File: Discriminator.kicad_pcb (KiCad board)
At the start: 2 copper layers, 29 parts, among them U1 PSA4-5043+, U2 PGA-103+

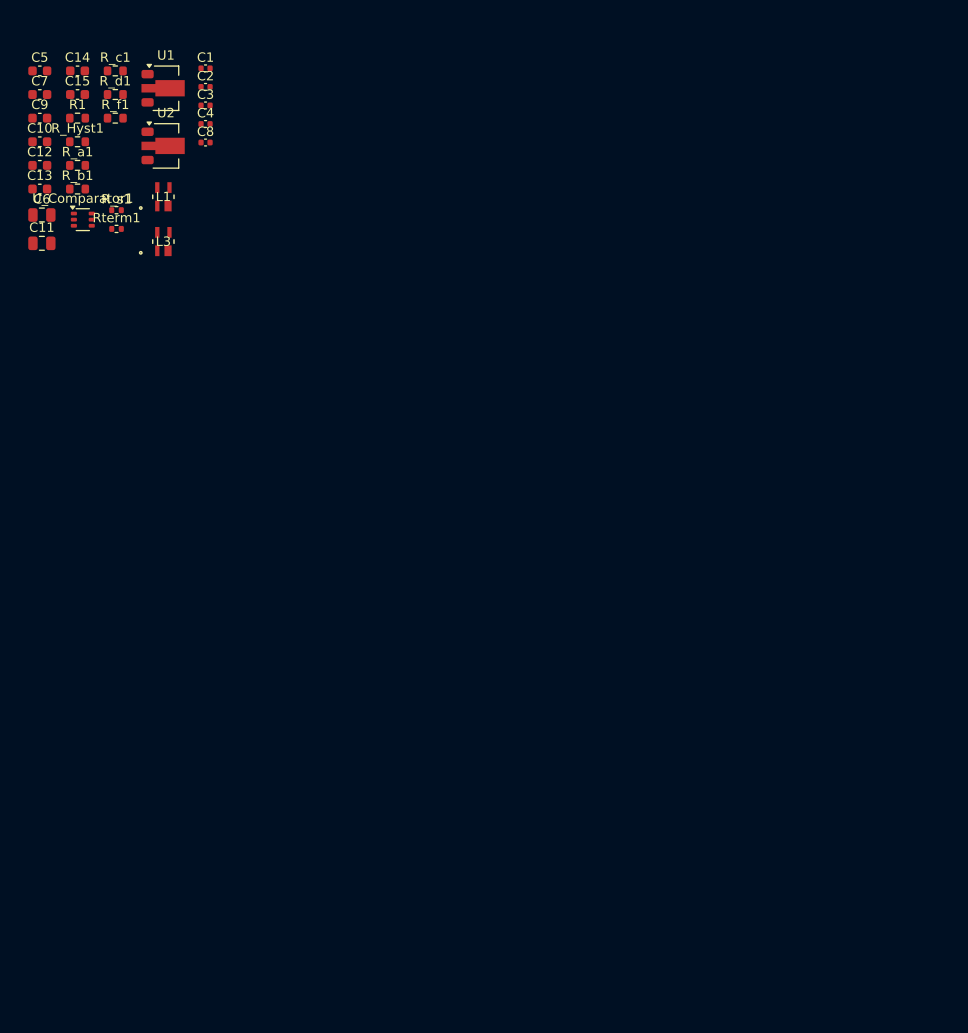
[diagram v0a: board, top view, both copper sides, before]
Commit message: added mcu section, added test points to CTD
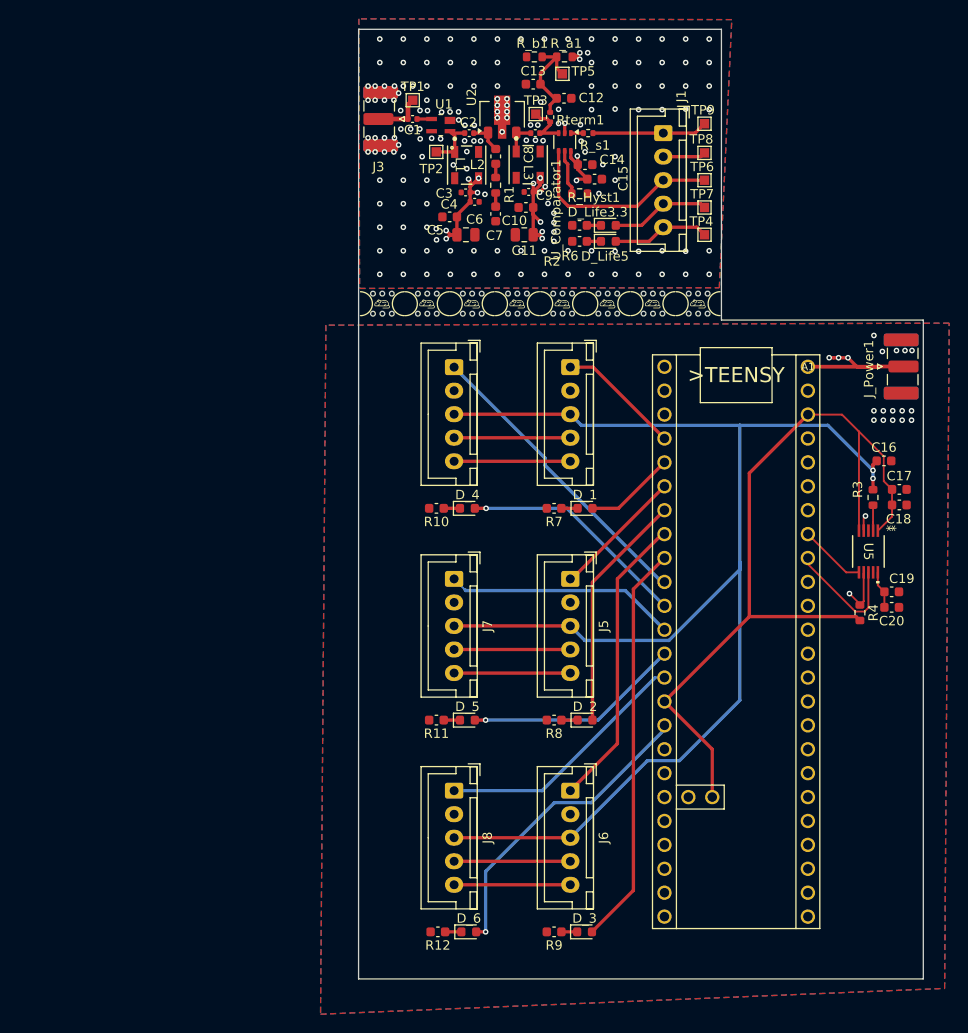
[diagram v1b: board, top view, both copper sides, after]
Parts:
- removed R_c1: 5.6k, Resistor_SMD:R_0603_1608Metric
- removed R_d1, R_f1: 1k, Resistor_SMD:R_0603_1608Metric
- added A1: TEENSY_4.1, TEENSY_4.1:TEENSY_LONG_EXT, F.Cu at (168.0, 62.3)
- added C16: 0.1uf, Capacitor_SMD:C_0603_1608Metric, F.Cu at (176.1, 72.3)
- added C17: 1uf, Capacitor_SMD:C_0603_1608Metric, F.Cu at (177.7, 75.4)
- added C18: 0.1uf, Capacitor_SMD:C_0603_1608Metric, F.Cu at (177.7, 77.0)
- added C19: 1uf, Capacitor_SMD:C_0603_1608Metric, F.Cu at (176.9, 86.2)
- added C20: 0.1uf, Capacitor_SMD:C_0603_1608Metric, F.Cu at (176.9, 87.9)
- added D_1: LED, LED_SMD:LED_0603_1608Metric, F.Cu at (144.3, 77.4)
- added D_2: LED, LED_SMD:LED_0603_1608Metric, F.Cu at (144.3, 99.9)
- added D_3: LED, LED_SMD:LED_0603_1608Metric, F.Cu at (144.3, 122.4)
- added D_4: LED, LED_SMD:LED_0603_1608Metric, F.Cu at (131.8, 77.4)
- added D_5: LED, LED_SMD:LED_0603_1608Metric, F.Cu at (131.8, 99.9)
- added D_6: LED, LED_SMD:LED_0603_1608Metric, F.Cu at (132.0, 122.4)
- added D_Life3.3: LED, LED_SMD:LED_0603_1608Metric, F.Cu at (146.8, 47.3)
- added D_Life5: LED, LED_SMD:LED_0603_1608Metric, F.Cu at (146.8, 49.0)
- added J1: Conn_01x05_Socket, Connector_JST:JST_XH_B5B-XH-A_1x05_P2.50mm_Vertical, F.Cu at (152.6, 37.5)
- added J2: Conn_01x05_Socket, Connector_JST:JST_XH_B5B-XH-A_1x05_P2.50mm_Vertical, F.Cu at (142.7, 62.4)
- added J3: Conn_Coaxial, Connector_Coaxial:SMA_Samtec_SMA-J-P-H-ST-EM1_EdgeMount, F.Cu at (122.3, 36.0)
- added J4: Conn_01x05_Socket, Connector_JST:JST_XH_B5B-XH-A_1x05_P2.50mm_Vertical, F.Cu at (130.4, 62.4)
- added J5: Conn_01x05_Socket, Connector_JST:JST_XH_B5B-XH-A_1x05_P2.50mm_Vertical, F.Cu at (142.7, 84.9)
- added J6: Conn_01x05_Socket, Connector_JST:JST_XH_B5B-XH-A_1x05_P2.50mm_Vertical, F.Cu at (142.7, 107.4)
- added J7: Conn_01x05_Socket, Connector_JST:JST_XH_B5B-XH-A_1x05_P2.50mm_Vertical, F.Cu at (130.4, 84.9)
- added J8: Conn_01x05_Socket, Connector_JST:JST_XH_B5B-XH-A_1x05_P2.50mm_Vertical, F.Cu at (130.4, 107.4)
- added J_Power1: Conn_Coaxial, Connector_Coaxial:SMA_Samtec_SMA-J-P-H-ST-EM1_EdgeMount, F.Cu at (178.1, 62.3)
- added L2: 620nH, Inductor_SMD:L_0603_1608Metric, F.Cu at (134.8, 40.0)
- added R10: 2k, Capacitor_SMD:C_0603_1608Metric, F.Cu at (128.5, 77.4)
- added R11: 2k, Capacitor_SMD:C_0603_1608Metric, F.Cu at (128.5, 99.9)
- added R12: 2k, Capacitor_SMD:C_0603_1608Metric, F.Cu at (128.7, 122.4)
- added R2: 2k, Capacitor_SMD:C_0603_1608Metric, F.Cu at (143.7, 47.3)
- added R3: 1k, Resistor_SMD:R_0603_1608Metric, F.Cu at (174.9, 76.2)
- added R4: 4.7k, Resistor_SMD:R_0603_1608Metric, F.Cu at (173.5, 88.5)
- added R6: 2k, Capacitor_SMD:C_0603_1608Metric, F.Cu at (143.7, 49.0)
- added R7: 2k, Capacitor_SMD:C_0603_1608Metric, F.Cu at (141.0, 77.4)
- added R8: 2k, Capacitor_SMD:C_0603_1608Metric, F.Cu at (141.0, 99.9)
- added R9: 2k, Capacitor_SMD:C_0603_1608Metric, F.Cu at (141.0, 122.4)
- added TP1: TestPoint, TestPoint:TestPoint_Pad_1.0x1.0mm, F.Cu at (126.0, 34.0)
- added TP2: TestPoint, TestPoint:TestPoint_Pad_1.0x1.0mm, F.Cu at (128.5, 39.5)
- added TP3: TestPoint, TestPoint:TestPoint_Pad_1.0x1.0mm, F.Cu at (139.1, 35.5)
- added TP4: TestPoint, TestPoint:TestPoint_Pad_1.0x1.0mm, F.Cu at (157.0, 48.3)
- added TP5: TestPoint, TestPoint:TestPoint_Pad_1.0x1.0mm, F.Cu at (141.9, 31.2)
- added TP6: TestPoint, TestPoint:TestPoint_Pad_1.0x1.0mm, F.Cu at (157.0, 42.5)
- added TP7: TestPoint, TestPoint:TestPoint_Pad_1.0x1.0mm, F.Cu at (157.0, 45.4)
- added TP8: TestPoint, TestPoint:TestPoint_Pad_1.0x1.0mm, F.Cu at (157.0, 39.6)
- added TP9: TestPoint, TestPoint:TestPoint_Pad_1.0x1.0mm, F.Cu at (157.0, 36.5)
- added U5: DAC60501-0x49, DAC60501ZDGSR:DGS10_TEX, F.Cu at (174.4, 82.0)
- added mouse-bite-2.54mm-4.66mm: VAL**, mouse-bite.pretty-main:mouse-bite-2.54mm-4.66mm, F.Cu at (151.5, 55.6)
- added mouse-bite-2.54mm-4.66mm: VAL**, mouse-bite.pretty-main:mouse-bite-2.54mm-4.66mm, F.Cu at (132.3, 55.6)
- added mouse-bite-2.54mm-4.66mm: VAL**, mouse-bite.pretty-main:mouse-bite-2.54mm-4.66mm, F.Cu at (137.1, 55.6)
- added mouse-bite-2.54mm-4.66mm: VAL**, mouse-bite.pretty-main:mouse-bite-2.54mm-4.66mm, F.Cu at (141.9, 55.6)
- added mouse-bite-2.54mm-4.66mm: VAL**, mouse-bite.pretty-main:mouse-bite-2.54mm-4.66mm, F.Cu at (156.3, 55.6)
- added mouse-bite-2.54mm-4.66mm: VAL**, mouse-bite.pretty-main:mouse-bite-2.54mm-4.66mm, F.Cu at (146.7, 55.6)
- added mouse-bite-2.54mm-4.66mm: VAL**, mouse-bite.pretty-main:mouse-bite-2.54mm-4.66mm, F.Cu at (127.5, 55.6)
- added mouse-bite-2.54mm-4.66mm: VAL**, mouse-bite.pretty-main:mouse-bite-2.54mm-4.66mm, F.Cu at (122.8, 55.6)
- C9: footprint Capacitor_SMD:C_0603_1608Metric -> Capacitor_SMD:C_0402_1005Metric
- L1, L3: footprint TCCH-80+:MMM1362_MNC -> TCCH+:GU1604_MNC
- U1: footprint Package_TO_SOT_SMD:SOT-89-3 -> PSA4-5043+:MMM1362_MNC
- moved C12 56.2 mm to (142.1, 33.8)
- moved C15 55.7 mm to (145.3, 42.4)
- moved C14 54.8 mm to (144.3, 40.9)
- moved R_Hyst1 53.6 mm to (143.7, 43.9)
- moved C13 53.6 mm to (138.8, 32.3), turned to 180 degrees
- moved R_a1 53.0 mm to (142.1, 29.4)
- moved C9 52.5 mm to (138.3, 43.8), turned to 180 degrees
- moved C10 52.1 mm to (138.0, 45.4), turned to 180 degrees
- moved U_Comparator1 51.9 mm to (142.2, 38.5), turned to -90 degrees
- moved C11 51.3 mm to (137.8, 48.3), turned to 180 degrees
- moved R_s1 50.8 mm to (144.6, 37.5)
- moved R_b1 50.5 mm to (138.9, 29.4)
- moved C7 50.1 mm to (134.8, 46.1), turned to -90 degrees
- moved Rterm1 47.6 mm to (140.6, 35.8), turned to -90 degrees
- moved C5 46.2 mm to (129.9, 46.4), turned to 180 degrees
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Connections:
- L1 pad 1: +5V -> Net-(C2-Pad2)
- L1 pad 2: Net-(C2-Pad2) -> (no net)
- L1 pad 3: (no net) -> +5V
- L3 pad 1: +5V -> Net-(C8-Pad1)
- L3 pad 2: Net-(C8-Pad1) -> (no net)
- L3 pad 3: (no net) -> +5V
- R_s1 pad 2: /Detection -> /Pulse
- U_Comparator1 pad 4: Net-(U_Comparator1--) -> /V_threshold
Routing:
- net +3.3VA: track 0.00 -> 189.2 mm
- net +5VA: track 0.00 -> 162.5 mm, vias 0 -> 3
- net /V_r: track 0.00 -> 150.7 mm, vias 0 -> 2
- net Net-(D_3-A): track 0.00 -> 42.9 mm
- net +5V: track 0.00 -> 35.2 mm, vias 0 -> 12
- net Net-(A1-A10): track 0.00 -> 33.1 mm, vias 0 -> 1
- net /4: track 0.00 -> 32.0 mm
- net /3: track 0.00 -> 31.5 mm
- net /6: track 0.00 -> 27.3 mm
- net Net-(D_2-A): track 0.00 -> 25.5 mm
- net /5: track 0.00 -> 24.6 mm
- net Net-(D_4-A): track 0.00 -> 24.4 mm, vias 0 -> 1
- net Net-(A1-(SDO)D11): track 0.00 -> 23.1 mm, vias 0 -> 1
- net /V_threshold: track 0.00 -> 21.9 mm
- net +3.3V: track 0.00 -> 18.3 mm, vias 0 -> 4
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- added copper zone on In2.Cu, net +3.3V
- added copper zone on In2.Cu, net +5V
- added copper zone on B.Cu, net GND
- added copper zone on F.Cu, net GND
- added copper zone on In1.Cu, net GND
- added copper zone on B.Cu, net GNDA
- added copper zone on F.Cu, net GNDA
- added copper zone on In1.Cu, net GNDA
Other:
- board outline added: 60 x 100.9 mm
- copper layers 2 -> 4
